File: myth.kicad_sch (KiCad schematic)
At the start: 141 parts, among them J1 Conn_01x08_Male, J2 Conn_01x08_Male, J4 Conn_01x08_Male, J5 Conn_01x08_Male, J6 Conn_01x08_Male, U1 74AHC02, U10 74HC595, U100 74AHC08, U101 74LS32, U102 74LS08, U103 74HC00, U104 74LS08, U105 74AHC02, U106 74LS08, U107 74LS08, U108 74LS08, U109 74LS573, U11 74HC165, U110 74LS573, U111 74HC157, U112 74HC157, U113 74HC157, U114 74AHC08, U115 4002, U116 4072, U117 74LS573, U118 74HC02, U119 74LS573, U12 74AHC08, U120 74LS573, U121 74AHC273, U122 74HC157, U123 74LS32, U124 74AHC04, U125 74LS573, U126 74LS573, U127 74AHC08, U128 74LS27, U129 74HC00, U13 74HC238, U130 74AHC08, U131 74LS573, U133 4072, U134 4072, U14 74HC238, U15 74HC238, U16 4002, U17 74AHC273, U18 74LS32, U19 CD4532BE, U2 74AHC04, U20 74AHC138, U21 74AHC04, U22 74AHC138, U23 74HC238, U24 74HC238, U25 74LS32, U26 4078, U27 74AHC244, U28 74HC238, U29 74HC238, U3 74HC74, U30 4075, U31 74AHC04, U32 74HC00, U33 74HC163, U34 74AHC138, U35 74AHC138, U36 74HC238, U37 74AHC138, U38 74LS32, U39 74HC238, U40 74AHC02, U41 74AHC574, U42 74LS573, U43 74HC157, U44 74HC157, U45 74HC193, U46 74HC193, U47 74AHC138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

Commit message: Add IOK instruction
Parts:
- removed unit 4 of U9
- added U132: 74HC74, Package_DIP:DIP-14_W7.62mm_Socket_LongPads, symbol 74xx:74HC74
- added U4: 74LS11, symbol 74xx:74LS11
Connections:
- net ACK: now also U4.12
- net BUSY: now also U132.5 (Q); no longer U75.13
- net GND: now also U132.3 (C)
- net VCC: now also U132.2 (D)
- net ~{IOK}: now reaches U20.9 (O6)
- net ~{IOK}: now also U132.1 (~{R})
- net at U63.5 (Q): now also U4.2
- net at U75.1: now also U4.1
- new net: U132.6 (~{Q}), U4.13
- new net ~{ACK}: U132.4 (~{S})
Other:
- note added: "Interrupts disabled when "BUSY" and when running code in page 0 (See code page index reg schematics bottom right)"
- note added: "TRAP opcode triggers call to interrupt service routine in page 0, disabling further interrupts, and toggles ("BUSY") BUSY state removed by IOK (Interrupts OK) instruction"
- note removed: "Interrupts disabled ("busy") when running code in page 0 (See code page index reg schematics bottom right)"
- note removed: "TRAP instruction calls interrupt service routine in page 0 ("busy"), disabling further interrupts and nesting"
- moved on the sheet: U123A, U63A

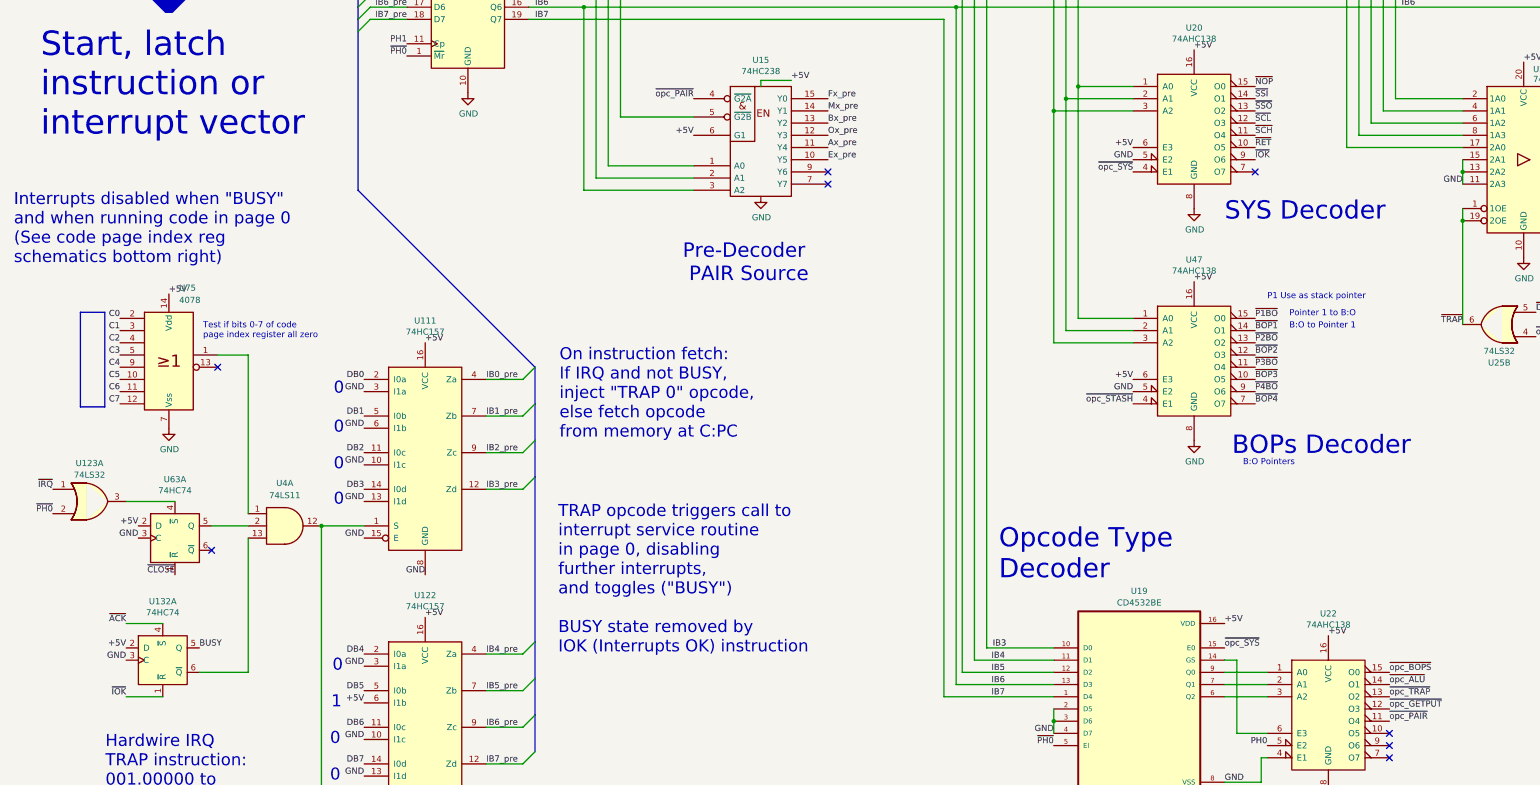
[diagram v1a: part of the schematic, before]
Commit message: Move IOK to RTI instruction, identical to RET
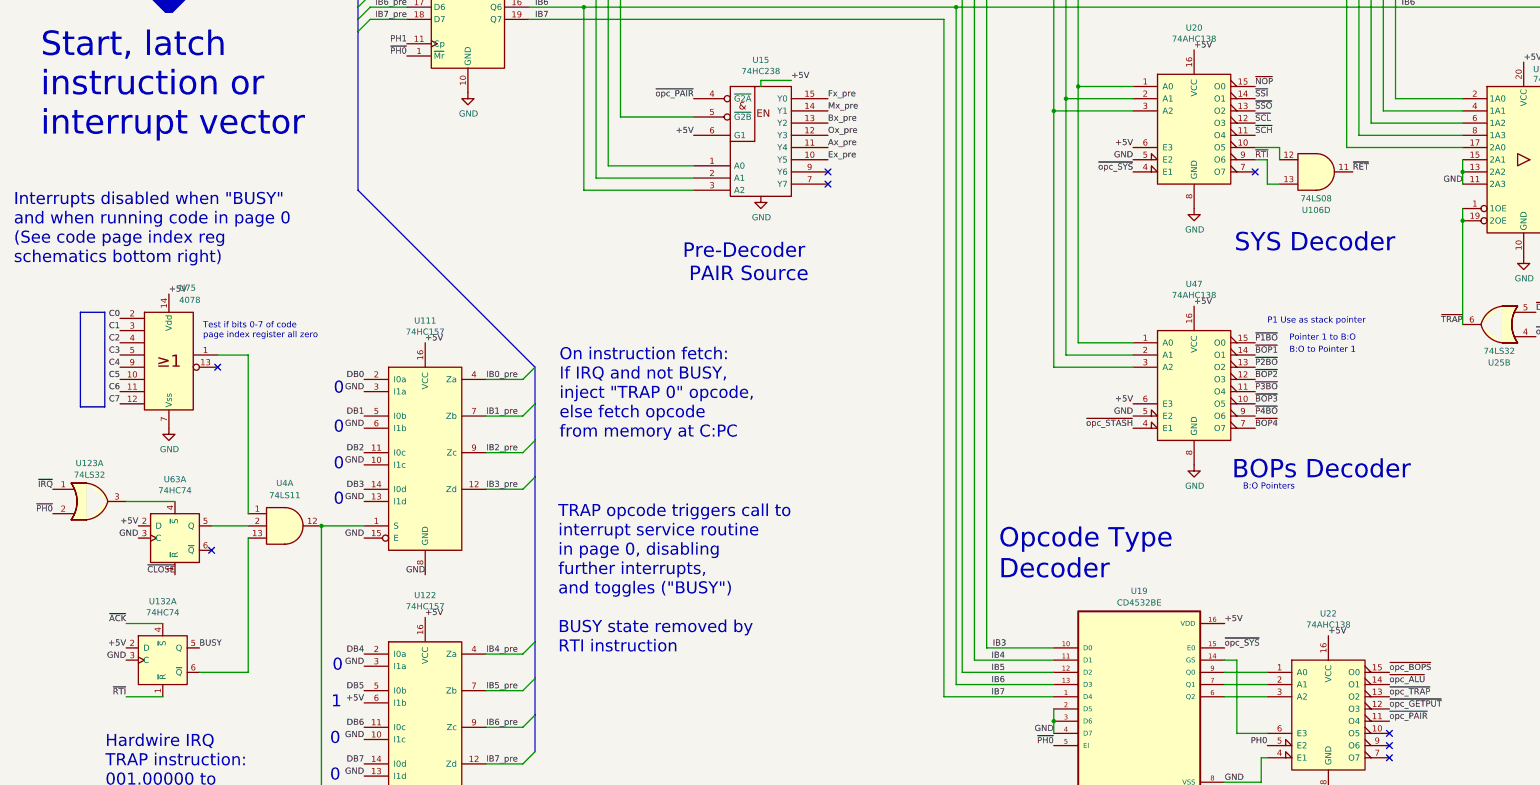
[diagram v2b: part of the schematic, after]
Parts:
- added unit 4 of U106
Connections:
- net ~{RET}: now also U106.11; no longer U20.10 (O5)
- net ~{IOK} renamed ~{RTI}
- net ~{RTI}: now also U106.13
- new net: U106.12, U20.10 (O5)
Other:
- note added: "TRAP opcode triggers call to interrupt service routine in page 0, disabling further interrupts, and toggles ("BUSY") BUSY state removed by RTI instruction"
- note removed: "TRAP opcode triggers call to interrupt service routine in page 0, disabling further interrupts, and toggles ("BUSY") BUSY state removed by IOK (Interrupts OK) instruction"
- moved on the sheet: U47

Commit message: Name P4 stack pointer
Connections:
- net ~{RTI}: now also U20.7 (O7); no longer U20.9 (O6)
- net at U20.10 (O5): no longer U106.12
- net BOP4 renamed BOSP
- net ~{BOP4} renamed ~{BOSP}
- net ~{P4BO} renamed ~{SPBO}
- new net: U106.12, U20.9 (O6)
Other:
- note added: "P4 use as stack pointer"
- note added: "~{BOP4}"
- note added: "~{P4BO}"
- note removed: "P1 Use as stack pointer"
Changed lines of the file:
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@@
 		)
 	)
+	(text "P4 use as stack pointer"
+		(exclude_from_sim no)
+		(at 311.15 459.486 0)
+		(effects
+			(font
+				(size 1.27 1.27)
+			)
+			(justify left bottom)
+		)
+	)
 	(text "573!\nTransparent\nLatch follows\ninput"
 		(exclude_from_sim no)
@@
 		)
 	)
-	(text "P1 Use as stack pointer"
+	(text "~{P4BO}"
 		(exclude_from_sim no)
-		(at 298.45 440.69 0)
+		(at 295.91 459.486 0)
 		(effects
 			(font
@@
 		)
 	)
+	(text "~{BOP4}"
+		(exclude_from_sim no)
+		(at 295.91 462.28 0)
+		(effects
+			(font
+				(size 1.27 1.27)
+			)
+			(justify left bottom)
+		)
+	)
 	(text " 8 AND (\"A boolean-and T\")\n 9 IOR (\"A inclusive-or T\")\n10 EOR (\"A exclusive-or T\")\n11 ADD (\"Add T to A)\n12 CAR (\"Carry bit of: A plus T\")\n13 AL_ (\"Is A less than T\")\n14 AE_ (\"Is A equal to T\")\n15 AG_ (\"Is A greater than T\")"
 		(exclude_from_sim no)
@@
 	)
 	(no_connect
-		(at 295.91 408.94)
+		(at 295.91 403.86)
 	)
 	(no_connect
@@
 		)
 	)
-	(wire
-		(pts
-			(xy 298.45 406.4) (xy 298.45 411.48)
-		)
-		(stroke
-			(width 0)
-			(type default)
-		)
-	)
 	(bus
 		(pts
@@
 	(wire
 		(pts
+			(xy 295.91 408.94) (xy 298.45 408.94)
+		)
+		(stroke
+			(width 0)
+			(type default)
+		)
+	)
+	(wire
+		(pts
 			(xy 408.94 186.69) (xy 407.67 186.69)
 		)
@@
 	(wire
 		(pts
-			(xy 295.91 406.4) (xy 298.45 406.4)
-		)
-		(stroke
-			(width 0)
-			(type default)
-		)
-	)
-	(wire
-		(pts
 			(xy 364.49 723.9) (xy 374.65 723.9)
 		)
@@
 		)
 	)
-	(wire
-		(pts
-			(xy 300.99 403.86) (xy 300.99 406.4)
-		)
-		(stroke
-			(width 0)
-			(type default)
-		)
-	)
 	(bus
 		(pts
@@
 	(wire
 		(pts
+			(xy 298.45 408.94) (xy 298.45 411.48)
+		)
+		(stroke
+			(width 0)
+			(type default)
+		)
+	)
+	(wire
+		(pts
 			(xy 1045.21 166.37) (xy 1055.37 156.21)
 		)
@@
 	(wire
 		(pts
+			(xy 295.91 459.74) (xy 304.8 459.74)
+		)
+		(stroke
+			(width 0)
+			(type default)
+		)
+	)
+	(wire
+		(pts
 			(xy 513.08 734.06) (xy 513.08 720.09)
 		)
@@
 		)
 	)
+	(wire
+		(pts
+			(xy 295.91 406.4) (xy 300.99 406.4)
+		)
+		(stroke
+			(width 0)
+			(type default)
+		)
+	)
 	(bus
 		(pts
@@
 	(wire
 		(pts
+			(xy 295.91 462.28) (xy 304.8 462.28)
+		)
+		(stroke
+			(width 0)
+			(type default)
+		)
+	)
+	(wire
+		(pts
 			(xy 161.29 346.71) (xy 161.29 364.49)
 		)
@@
 		)
 	)
-	(wire
-		(pts
-			(xy 295.91 403.86) (xy 300.99 403.86)
-		)
-		(stroke
-			(width 0)
-			(type default)
-		)
-	)
 	(bus
 		(pts
@@
 		)
 	)
-	(label "BOP4"
+	(label "BOSP"
 		(at 1120.14 378.46 180)
 		(effects
@@
 		)
 	)
-	(label "~{P4BO}"
+	(label "~{SPBO}"
 		(at 1120.14 381 180)
 		(effects
@@
 		)
 	)
-	(label "~{P4BO}"
-		(at 295.91 459.74 0)
-		(effects
-			(font
-				(size 1.27 1.27)
-			)
-			(justify left bottom)
-		)
-	)
 	(label "DB2"
 		(at 904.24 77.47 180)
@@
 		)
 	)
+	(label "~{SPBO}"
+		(at 304.8 459.74 0)
+		(effects
+			(font
+				(size 1.27 1.27)
+			)
+			(justify left bottom)
+		)
+	)
 	(label "D7"
 		(at 612.14 184.15 0)
@@
 		)
 	)
+	(label "~{BOSP}"
+		(at 304.8 462.28 0)
+		(effects
+			(font
+				(size 1.27 1.27)
+			)
+			(justify left bottom)
+		)
+	)
 	(label "DB6"
 		(at 1145.54 370.84 0)
@@
 		)
 	)
-	(label "BOP4"
+	(label "BOSP"
 		(at 1064.26 378.46 180)
 		(effects
@@
 		)
 	)
-	(label "~{BOP4}"
-		(at 295.91 462.28 0)
-		(effects
-			(font
-				(size 1.27 1.27)
-			)
-			(justify left bottom)
-		)
-	)
 	(label "GND"
 		(at 274.32 652.78 180)
@@
 		)
 	)
-	(label "~{P4BO}"
+	(label "~{SPBO}"
 		(at 1064.26 381 180)
 		(effects
@@
 	)
 	(label "~{RTI}"
-		(at 295.91 406.4 0)
+		(at 295.91 408.94 0)
 		(effects
 			(font

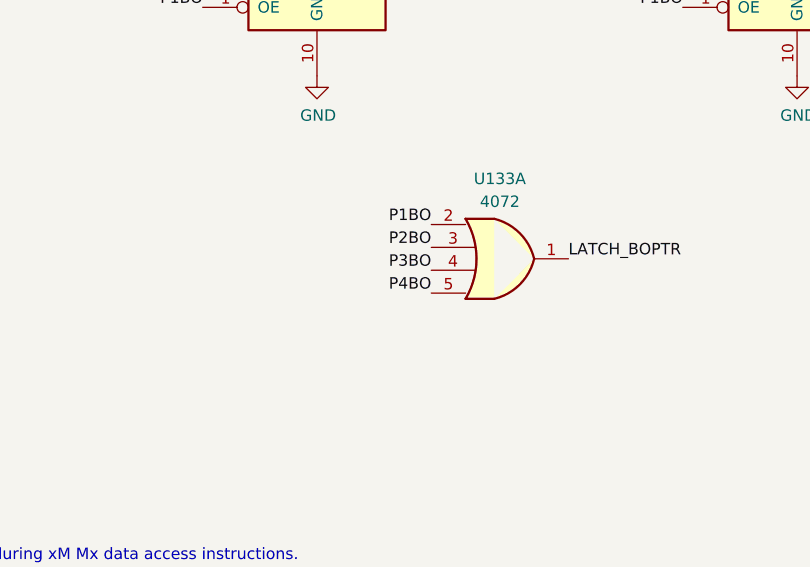
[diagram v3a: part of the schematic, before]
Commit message: Change incorrect signal label
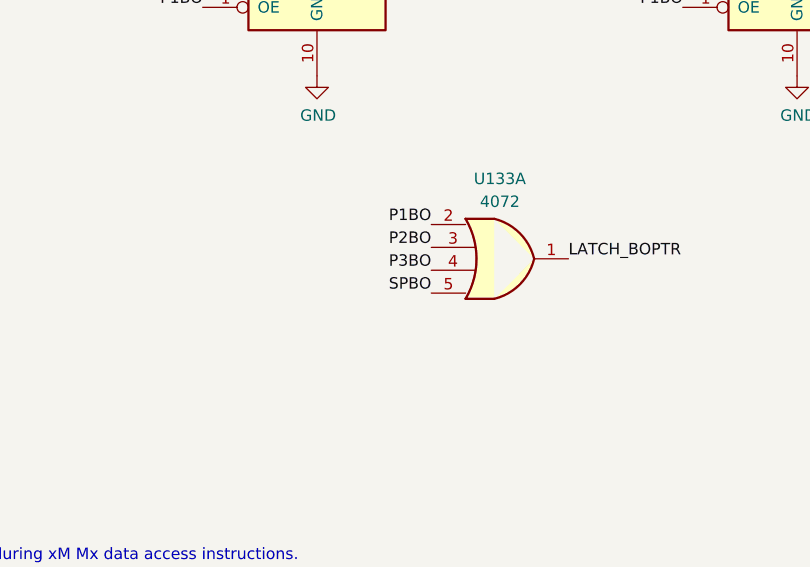
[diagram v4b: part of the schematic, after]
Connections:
- net P4BO renamed SPBO
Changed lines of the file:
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@@
 		)
 	)
-	(label "P4BO"
+	(label "SPBO"
 		(at 1089.66 600.71 180)
 		(effects

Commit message: Rename RET to RTS, to match RTI
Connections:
- net RET renamed RTS
- net ~{RET} renamed ~{RTS}
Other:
- note added: "B: - Saves page index of current instruction byte during call/trap/go - Outputs RTSurn page index during RTS - Is the implied page index for memory read-write, with the corresponding byte offset stored in O (Offset) - Together with O forms a 16-bit address pointers subject to the xU instruction The B:O pointer can be loaded from/saved into the BO-Pointers P1-4"
- note added: "O: - Saves offset of current instruction byte during call/trap/go - Outputs RTSurn offset during RTS - Is the (only!) implied address offset for memory read-write, with the corresponding page index stored in B (Base) - Together with B forms 16-bit address pointers subject to the xU instruction. The B:O pointer can be loaded from/saved into the BO-Pointers P1-4"
- note added: "On EXIT (SUBR/xG): Save code page index into B for RTSurn"
- note added: "On EXIT (SUBR/xG): Save code page offset into O for RTSurn"
- note added: "On RTS/xG/xC: Load instruction offset from O into PC"
- note added: "On RTS: Restore PC value from O register (Center right)"
- note added: "Register at CLOSE xU instruction adder would feedback B0-7 goes to PC module latched during RTS"
- note added: "The L register is decremented during CALL/TRAP/ENTER and incremented during RTS/LEAVE This operations provide single-page local stack frames for nested subroutines. Each local page has "GETPUT" variables called L0-L7 at byte offsets 0xF8-0xFF."
- note removed: "B: - Saves page index of current instruction byte during call/trap/go - Outputs return page index during RET - Is the implied page index for memory read-write, with the corresponding byte offset stored in O (Offset) - Together with O forms a 16-bit address pointers subject to the xU instruction The B:O pointer can be loaded from/saved into the BO-Pointers P1-4"
- note removed: "O: - Saves offset of current instruction byte during call/trap/go - Outputs return offset during RET - Is the (only!) implied address offset for memory read-write, with the corresponding page index stored in B (Base) - Together with B forms 16-bit address pointers subject to the xU instruction. The B:O pointer can be loaded from/saved into the BO-Pointers P1-4"
- note removed: "On EXIT (SUBR/xG): Save code page index into B for return"
- note removed: "On EXIT (SUBR/xG): Save code page offset into O for return"
- note removed: "On RET/xG/xC: Load instruction offset from O into PC"
- note removed: "On RET: Restore PC value from O register (Center right)"
- note removed: "Register at CLOSE xU instruction adder would feedback B0-7 goes to PC module latched during RET"
- note removed: "The L register is decremented during CALL/TRAP/ENTER and incremented during RET/LEAVE This operations provide single-page local stack frames for nested subroutines. Each local page has "GETPUT" variables called L0-L7 at byte offsets 0xF8-0xFF."
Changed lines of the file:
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@@
 		)
 	)
-	(text "O:\n- Saves offset of current instruction byte during call/trap/go\n- Outputs return offset during RET\n- Is the (only!) implied address offset for memory read-write, with the corresponding page index stored in B (Base)\n- Together with B forms 16-bit address pointers subject to the xU instruction.\n  The B:O pointer can be loaded from/saved into the BO-Pointers P1-4"
+	(text "O:\n- Saves offset of current instruction byte during call/trap/go\n- Outputs RTSurn offset during RTS\n- Is the (only!) implied address offset for memory read-write, with the corresponding page index stored in B (Base)\n- Together with B forms 16-bit address pointers subject to the xU instruction.\n  The B:O pointer can be loaded from/saved into the BO-Pointers P1-4"
 		(exclude_from_sim no)
 		(at 773.176 389.89 0)
@@
 		)
 	)
-	(text "On RET/xG/xC:\nLoad instruction\noffset from O\ninto PC\n"
+	(text "On RTS/xG/xC:\nLoad instruction\noffset from O\ninto PC\n"
 		(exclude_from_sim no)
 		(at 566.674 302.514 0)
@@
 		)
 	)
-	(text "Register at CLOSE\nxU instruction adder\nwould feedback\n\nB0-7 goes to PC module\nlatched during RET"
+	(text "Register at CLOSE\nxU instruction adder\nwould feedback\n\nB0-7 goes to PC module\nlatched during RTS"
 		(exclude_from_sim no)
 		(at 1035.558 259.334 0)
@@
 		)
 	)
-	(text "On RET:\nRestore PC value\nfrom O register\n(Center right)"
+	(text "On RTS:\nRestore PC value\nfrom O register\n(Center right)"
 		(exclude_from_sim no)
 		(at 511.81 364.49 0)
@@
 		)
 	)
-	(text "On EXIT (SUBR/xG):\nSave code page\noffset into O\nfor return"
+	(text "On EXIT (SUBR/xG):\nSave code page\noffset into O\nfor RTSurn"
 		(exclude_from_sim no)
 		(at 883.666 324.612 0)
@@
 		)
 	)
-	(text "On EXIT (SUBR/xG):\nSave code page\nindex into B\nfor return"
+	(text "On EXIT (SUBR/xG):\nSave code page\nindex into B\nfor RTSurn"
 		(exclude_from_sim no)
 		(at 767.08 566.42 0)
@@
 		)
 	)
-	(text "The L register is decremented during CALL/TRAP/ENTER\nand incremented during RET/LEAVE\n\nThis operations provide single-page local\nstack frames for nested subroutines.\n\nEach local page has \"GETPUT\" variables called\nL0-L7 at byte offsets 0xF8-0xFF.\n"
+	(text "The L register is decremented during CALL/TRAP/ENTER\nand incremented during RTS/LEAVE\n\nThis operations provide single-page local\nstack frames for nested subroutines.\n\nEach local page has \"GETPUT\" variables called\nL0-L7 at byte offsets 0xF8-0xFF.\n"
 		(exclude_from_sim no)
 		(at 500.126 624.332 0)
@@
 		)
 	)
-	(text "B:\n- Saves page index of current instruction byte during call/trap/go\n- Outputs return page index during RET\n- Is the implied page index for memory read-write, with the corresponding byte offset stored in O (Offset)\n- Together with O forms a 16-bit address pointers subject to the xU instruction\n  The B:O pointer can be loaded from/saved into the BO-Pointers P1-4"
+	(text "B:\n- Saves page index of current instruction byte during call/trap/go\n- Outputs RTSurn page index during RTS\n- Is the implied page index for memory read-write, with the corresponding byte offset stored in O (Offset)\n- Together with O forms a 16-bit address pointers subject to the xU instruction\n  The B:O pointer can be loaded from/saved into the BO-Pointers P1-4"
 		(exclude_from_sim no)
 		(at 748.284 608.838 0)
@@
 		)
 	)
-	(label "RET"
+	(label "RTS"
 		(at 615.95 326.39 180)
 		(effects
@@
 		)
 	)
-	(label "~{RET}"
+	(label "~{RTS}"
 		(at 497.84 720.09 180)
 		(effects
@@
 		)
 	)
-	(label "~{RET}"
+	(label "~{RTS}"
 		(at 316.23 408.94 0)
 		(effects

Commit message: Fix floating pins in scrounger
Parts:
- removed U26: 4078, Package_DIP:DIP-14_W7.62mm_Socket_LongPads, symbol 4xxx_IEEE:4078
- added U135: 4078, symbol 4xxx_IEEE:4078
- U58, U95: footprint Package_DIP:DIP-14_W7.62mm_Socket_LongPads -> (none)
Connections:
- net A0: now also U135.11; no longer U95.11
- net A1: now also U135.10; no longer U95.10
- net A2: now also U135.9; no longer U95.9
- net A3: now also U135.5; no longer U95.5
- net A4: now also U135.4; no longer U95.4
- net A5: now also U135.3; no longer U95.3
- net A6: now also U135.2; no longer U95.2
- net A7: now also U135.12; no longer U95.12
- net CODE: now also U95.12
- net DEC: now also U95.4
- net ENTER: now also U95.9
- net GND: now also U95.2, U95.3, U135.7 (Vss)
- net INC: now also U95.5
- net LEAVE: now also U95.10
- net LOCAL: now also U95.11
- net NZFLAG_A: now also U135.1; no longer U95.1
- net SCROUNGE: now also U30.11, U95.1; no longer U30.13
- net ZFLAG_A: now also U135.13; no longer U95.13
- net ~{PH3}: now also U30.13; no longer U30.12
- net ~{opc_PAIR}: now also U30.12; no longer U30.11
- no-connect marks 56 -> 47
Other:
- note removed: "PIN 1 (non-inverted output) was missing in KiCAD symbol"
- moved on the sheet: U30C
